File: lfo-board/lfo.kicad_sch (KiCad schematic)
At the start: 21 parts

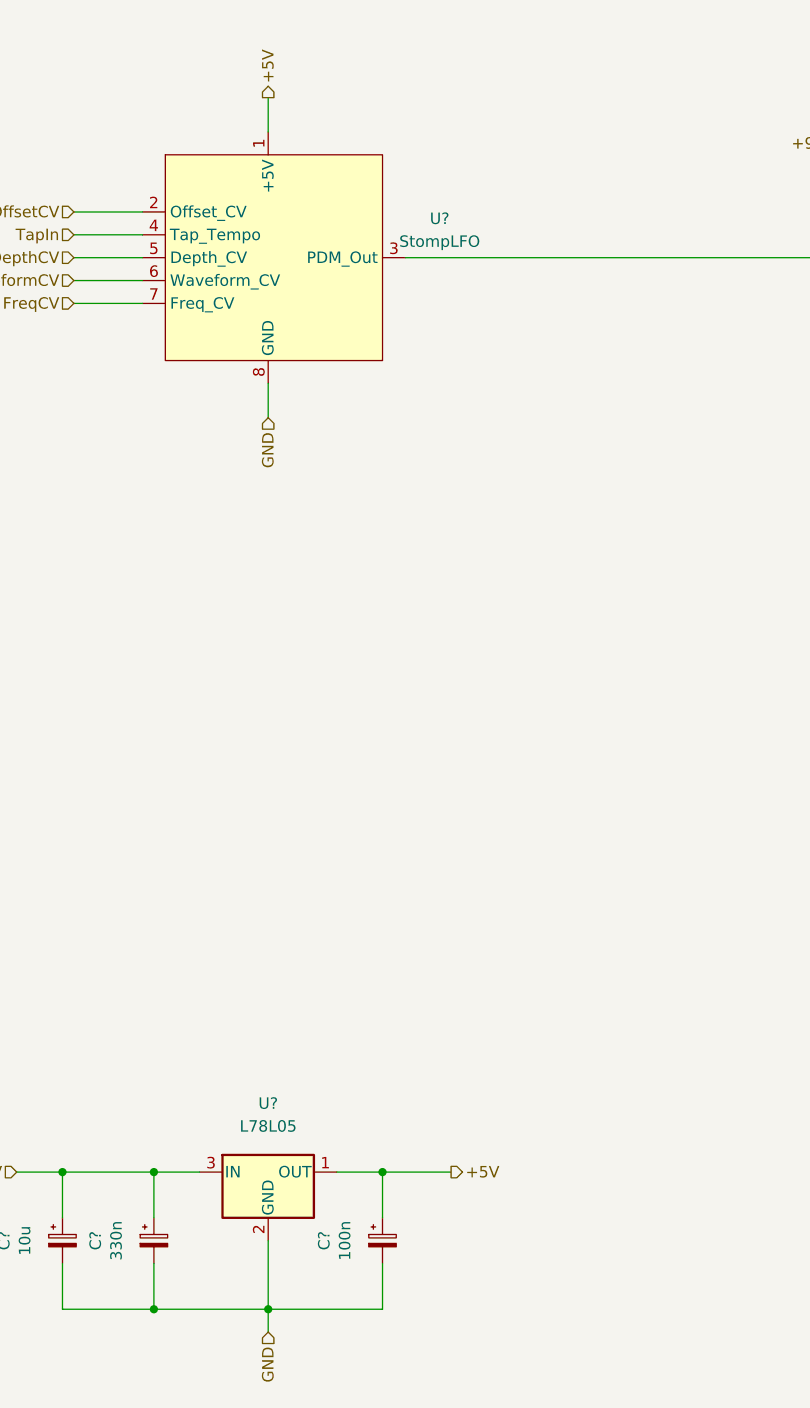
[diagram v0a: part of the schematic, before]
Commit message: IO Board wip
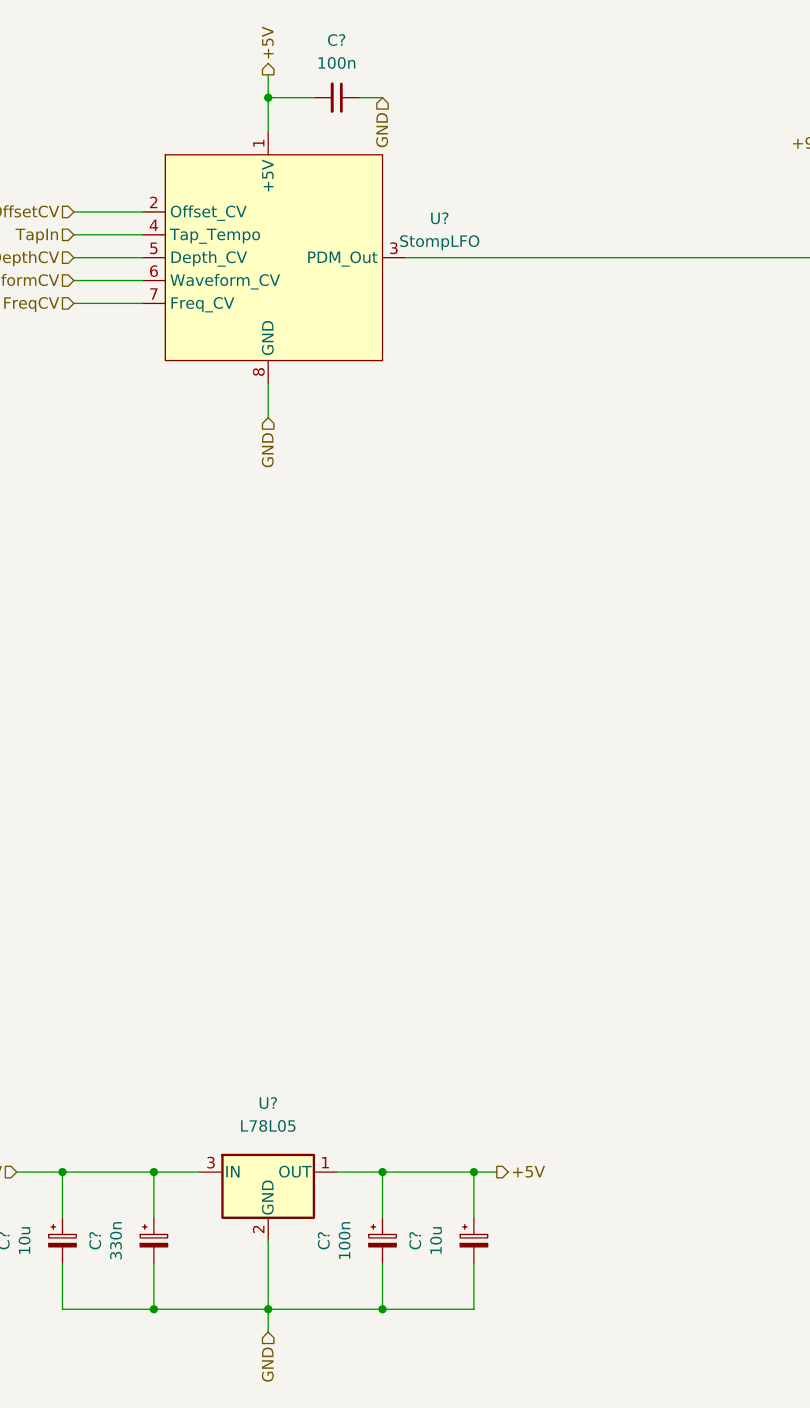
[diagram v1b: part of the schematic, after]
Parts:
- added C?: 10u, Capacitor_Tantalum_SMD:CP_EIA-3216-10_Kemet-I_Pad1.58x1.35mm_HandSolder, symbol Device:C_Polarized_Small
- added C?: 100n, symbol Device:C_Small
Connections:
- net +5V: now also C?.1, C?.2
- net GND: now also C?.1, C?.2
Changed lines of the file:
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@@
   (junction (at 66.04 152.4) (diameter 0) (color 0 0 0 0)
   )
+  (junction (at 91.44 167.64) (diameter 0) (color 0 0 0 0)
+  )
+  (junction (at 78.74 33.02) (diameter 0) (color 0 0 0 0)
+  )
   (junction (at 170.18 50.8) (diameter 0) (color 0 0 0 0)
   )
@@
   (junction (at 203.2 53.34) (diameter 0) (color 0 0 0 0)
   )
+  (junction (at 101.6 152.4) (diameter 0) (color 0 0 0 0)
+  )
   (junction (at 193.04 66.04) (diameter 0) (color 0 0 0 0)
   )
@@
     (stroke (width 0) (type default) (color 0 0 0 0))
   )
+  (wire (pts (xy 101.6 152.4) (xy 101.6 157.48))
+    (stroke (width 0) (type default) (color 0 0 0 0))
+  )
   (wire (pts (xy 154.94 50.8) (xy 160.02 50.8))
     (stroke (width 0) (type default) (color 0 0 0 0))
@@
     (stroke (width 0) (type default) (color 0 0 0 0))
   )
-  (wire (pts (xy 91.44 152.4) (xy 99.06 152.4))
+  (wire (pts (xy 91.44 152.4) (xy 101.6 152.4))
     (stroke (width 0) (type default) (color 0 0 0 0))
   )
@@
     (stroke (width 0) (type default) (color 0 0 0 0))
   )
+  (wire (pts (xy 101.6 167.64) (xy 91.44 167.64))
+    (stroke (width 0) (type default) (color 0 0 0 0))
+  )
   (wire (pts (xy 182.88 109.22) (xy 177.8 109.22))
     (stroke (width 0) (type default) (color 0 0 0 0))
   )
+  (wire (pts (xy 78.74 33.02) (xy 83.82 33.02))
+    (stroke (width 0) (type default) (color 0 0 0 0))
+  )
   (wire (pts (xy 187.96 109.22) (xy 193.04 109.22))
     (stroke (width 0) (type default) (color 0 0 0 0))
   )
+  (wire (pts (xy 101.6 162.56) (xy 101.6 167.64))
+    (stroke (width 0) (type default) (color 0 0 0 0))
+  )
+  (wire (pts (xy 88.9 33.02) (xy 91.44 33.02))
+    (stroke (width 0) (type default) (color 0 0 0 0))
+  )
+  (wire (pts (xy 78.74 30.48) (xy 78.74 33.02))
+    (stroke (width 0) (type default) (color 0 0 0 0))
+  )
+  (wire (pts (xy 170.18 50.8) (xy 177.8 50.8))
+    (stroke (width 0) (type default) (color 0 0 0 0))
+  )
+  (wire (pts (xy 187.96 99.06) (xy 193.04 99.06))
+    (stroke (width 0) (type default) (color 0 0 0 0))
+  )
+  (wire (pts (xy 193.04 99.06) (xy 193.04 109.22))
+    (stroke (width 0) (type default) (color 0 0 0 0))
+  )
+  (wire (pts (xy 256.54 60.96) (xy 266.7 60.96))
+    (stroke (width 0) (type default) (color 0 0 0 0))
+  )
+  (wire (pts (xy 193.04 66.04) (xy 193.04 63.5))
+    (stroke (width 0) (type default) (color 0 0 0 0))
+  )
+  (wire (pts (xy 172.72 124.46) (xy 177.8 124.46))
+    (stroke (width 0) (type default) (color 0 0 0 0))
+  )
+  (wire (pts (xy 203.2 63.5) (xy 210.82 63.5))
+    (stroke (width 0) (type default) (color 0 0 0 0))
+  )
   (wire (pts (xy 78.74 33.02) (xy 78.74 36.83))
     (stroke (width 0) (type default) (color 0 0 0 0))
   )
-  (wire (pts (xy 170.18 50.8) (xy 177.8 50.8))
-    (stroke (width 0) (type default) (color 0 0 0 0))
-  )
-  (wire (pts (xy 187.96 99.06) (xy 193.04 99.06))
-    (stroke (width 0) (type default) (color 0 0 0 0))
-  )
-  (wire (pts (xy 193.04 99.06) (xy 193.04 109.22))
-    (stroke (width 0) (type default) (color 0 0 0 0))
-  )
-  (wire (pts (xy 256.54 60.96) (xy 266.7 60.96))
-    (stroke (width 0) (type default) (color 0 0 0 0))
-  )
-  (wire (pts (xy 193.04 66.04) (xy 193.04 63.5))
-    (stroke (width 0) (type default) (color 0 0 0 0))
-  )
-  (wire (pts (xy 172.72 124.46) (xy 177.8 124.46))
-    (stroke (width 0) (type default) (color 0 0 0 0))
-  )
-  (wire (pts (xy 203.2 63.5) (xy 210.82 63.5))
-    (stroke (width 0) (type default) (color 0 0 0 0))
-  )
   (wire (pts (xy 55.88 167.64) (xy 66.04 167.64))
+    (stroke (width 0) (type default) (color 0 0 0 0))
+  )
+  (wire (pts (xy 101.6 152.4) (xy 104.14 152.4))
     (stroke (width 0) (type default) (color 0 0 0 0))
   )
@@
     (effects (font (size 1.27 1.27)) (justify right))
   )
+  (hierarchical_label "GND" (shape input) (at 91.44 33.02 270)
+    (effects (font (size 1.27 1.27)) (justify right))
+  )
   (hierarchical_label "Out" (shape input) (at 220.98 53.34 0)
     (effects (font (size 1.27 1.27)) (justify left))
@@
     (effects (font (size 1.27 1.27)) (justify left))
   )
-  (hierarchical_label "+5V" (shape output) (at 78.74 33.02 90)
+  (hierarchical_label "+5V" (shape output) (at 78.74 30.48 90)
     (effects (font (size 1.27 1.27)) (justify left))
   )
@@
     (effects (font (size 1.27 1.27)) (justify right))
   )
-  (hierarchical_label "+5V" (shape output) (at 99.06 152.4 0)
+  (hierarchical_label "+5V" (shape output) (at 104.14 152.4 0)
     (effects (font (size 1.27 1.27)) (justify left))
   )
@@
     )
     (property "Datasheet" "~" (id 3) (at 193.04 71.12 0)
+      (effects (font (size 1.27 1.27)) hide)
+    )
+    (pin "1")
+    (pin "2")
+  )
+  (symbol (lib_id "Device:C_Polarized_Small") (at 101.6 160.02 0) (unit 1)
+    (in_bom yes) (on_board yes)
+    (property "Reference" "C?" (id 0) (at 95.123 160.02 90))
+    (property "Value" "10u" (id 1) (at 97.4344 160.02 90))
+    (property "Footprint" "Capacitor_Tantalum_SMD:CP_EIA-3216-10_Kemet-I_Pad1.58x1.35mm_HandSolder" (id 2) (at 101.6 160.02 0)
+      (effects (font (size 1.27 1.27)) hide)
+    )
+    (property "Datasheet" "~" (id 3) (at 101.6 160.02 0)
+      (effects (font (size 1.27 1.27)) hide)
+    )
+    (property "LCSC" "C128254" (id 4) (at 101.6 160.02 0)
+      (effects (font (size 1.27 1.27)) hide)
+    )
+    (property "Role" "" (id 5) (at 101.6 160.02 0)
+      (effects (font (size 1.27 1.27)) hide)
+    )
+    (property "Mouser" "" (id 6) (at 101.6 160.02 0)
       (effects (font (size 1.27 1.27)) hide)
     )
@@
       (effects (font (size 1.27 1.27)) hide)
     )
+    (pin "1")
+    (pin "2")
+  )
+  (symbol (lib_id "Device:C_Small") (at 86.36 33.02 270) (unit 1)
+    (in_bom yes) (on_board yes) (fields_autoplaced)
+    (property "Reference" "C?" (id 0) (at 86.3536 26.67 90))
+    (property "Value" "100n" (id 1) (at 86.3536 29.21 90))
+    (property "Footprint" "" (id 2) (at 86.36 33.02 0)
+      (effects (font (size 1.27 1.27)) hide)
+    )
+    (property "Datasheet" "~" (id 3) (at 86.36 33.02 0)
+      (effects (font (size 1.27 1.27)) hide)
+    )

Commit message: wip
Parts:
- removed C?: 47n, symbol Device:C_Small
- removed R?: 1K, symbol Device:R_Small
- removed R?: 100K, symbol Device:R_Small
- added D2: LED_Dual_Bidirectional, LED_SMD:LED_0603_1608Metric_Pad1.05x0.95mm_HandSolder, symbol Device:LED_Dual_Bidirectional
- added R34: 470, Resistor_SMD:R_0603_1608Metric_Pad0.98x0.95mm_HandSolder, symbol Device:R_Small
- added R35: 20K, Resistor_SMD:R_0603_1608Metric_Pad0.98x0.95mm_HandSolder, symbol Device:R_Small
- C14, C17, C18, C19: renamed from C?; footprint (none) -> Capacitor_SMD:C_0603_1608Metric_Pad1.08x0.95mm_HandSolder
- R30, R31, R32, R33, R36, R37, R38: renamed from R?; footprint (none) -> Resistor_SMD:R_0603_1608Metric_Pad0.98x0.95mm_HandSolder
- U4, U6: renamed from U?; footprint (none) -> Package_SO:SOIC-8_3.9x4.9mm_P1.27mm
- gave numbers to parts that had none: 5
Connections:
- net +4.5V: now also R34.2, R35.1; no longer U6.5 (+)
- net at U6.6 (-): now also D2.2 (AK), R34.1; no longer R33.2
- net at U6.7: now also D2.1 (KA)
- new net: R33.2, R35.2, U6.5 (+)
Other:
- moved on the sheet: R33

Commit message: LFO graphics
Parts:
- C17: value 10n -> 6.8n
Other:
- note added: "C17 is 10n in the doc, switched due to tests w/ Konstrukt"
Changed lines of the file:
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@@
     (stroke (width 0) (type default) (color 0 0 0 0))
+  )
+  (text "C17 is 10n in the doc,\nswitched due to tests w/ Konstrukt"
+    (at 161.29 29.21 0)
+    (effects (font (size 1.27 1.27)) (justify left bottom))
   )
   (label "LFOFiltered" (at 162.56 124.46 180)
@@
     (in_bom yes) (on_board yes) (fields_autoplaced)
     (property "Reference" "C17" (id 0) (at 162.5663 31.75 90))
-    (property "Value" "10n" (id 1) (at 162.5663 34.29 90))
+    (property "Value" "6.8n" (id 1) (at 162.5663 34.29 90))
     (property "Footprint" "Capacitor_SMD:C_0603_1608Metric_Pad1.08x0.95mm_HandSolder" (id 2) (at 162.56 38.1 0)
       (effects (font (size 1.27 1.27)) hide)

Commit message: wip attenuverters
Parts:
- D2: footprint LED_SMD:LED_0603_1608Metric_Pad1.05x0.95mm_HandSolder -> LED_THT:LED_D3.0mm
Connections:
- net at R34.1, U6.6 (-): now also D2.1 (KA); no longer D2.2 (AK)
- net at U6.7: now also D2.2 (AK); no longer D2.1 (KA)
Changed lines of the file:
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@@
     (pin "2")
   )
-  (symbol (lib_id "Device:LED_Dual_Bidirectional") (at 185.42 99.06 0) (unit 1)
+  (symbol (lib_id "Device:LED_Dual_Bidirectional") (at 185.42 99.06 0) (mirror y) (unit 1)
     (in_bom yes) (on_board yes) (fields_autoplaced)
-    (property "Reference" "D2" (id 0) (at 185.9153 87.63 0))
-    (property "Value" "LED_Dual_Bidirectional" (id 1) (at 185.9153 90.17 0))
-    (property "Footprint" "LED_SMD:LED_0603_1608Metric_Pad1.05x0.95mm_HandSolder" (id 2) (at 185.42 99.06 0)
+    (property "Reference" "D2" (id 0) (at 184.9247 87.63 0))
+    (property "Value" "LED_Dual_Bidirectional" (id 1) (at 184.9247 90.17 0))
+    (property "Footprint" "LED_THT:LED_D3.0mm" (id 2) (at 185.42 99.06 0)
       (effects (font (size 1.27 1.27)) hide)
     )

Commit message: LFO board jlc
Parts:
- C14, C19: LCSC (none) -> C497032
- C17: value 6.8n -> 10n; LCSC (none) -> C57112
- C18: LCSC (none) -> C85980
- R30: LCSC (none) -> C23137
- R31: LCSC (none) -> C23242
- R32, R35: LCSC (none) -> C4184
- R33, R37: LCSC (none) -> C25803
- R34: value 470 -> 1k; LCSC (none) -> C21190
- R36: LCSC (none) -> C23352
- R38: LCSC (none) -> C21190
- U6: LCSC (none) -> C46127
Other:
- note removed: "C17 is 10n in the doc, switched due to tests w/ Konstrukt"
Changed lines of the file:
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@@
     (stroke (width 0) (type default) (color 0 0 0 0))
-  )
-  (text "C17 is 10n in the doc,\nswitched due to tests w/ Konstrukt"
-    (at 161.29 29.21 0)
-    (effects (font (size 1.27 1.27)) (justify left bottom))
   )
   (label "LFOFiltered" (at 162.56 124.46 180)
@@
     )
     (property "Datasheet" "~" (id 3) (at 193.04 71.12 0)
+      (effects (font (size 1.27 1.27)) hide)
+    )
+    (property "LCSC" "C25803" (id 4) (at 193.04 71.12 0)
       (effects (font (size 1.27 1.27)) hide)
     )
@@
       (effects (font (size 1.27 1.27)) hide)
     )
+    (property "LCSC" "C23137" (id 4) (at 149.86 38.1 0)
+      (effects (font (size 1.27 1.27)) hide)
+    )
     (pin "1")
     (pin "2")
@@
     )
     (property "Datasheet" "~" (id 3) (at 193.04 60.96 0)
+      (effects (font (size 1.27 1.27)) hide)
+    )
+    (property "LCSC" "C23352" (id 4) (at 193.04 60.96 0)
       (effects (font (size 1.27 1.27)) hide)
     )
@@
     (in_bom yes) (on_board yes) (fields_autoplaced)
     (property "Reference" "R34" (id 0) (at 171.45 92.71 90))
-    (property "Value" "470" (id 1) (at 171.45 95.25 90))
+    (property "Value" "1k" (id 1) (at 171.45 95.25 90))
     (property "Footprint" "Resistor_SMD:R_0603_1608Metric_Pad0.98x0.95mm_HandSolder" (id 2) (at 171.45 99.06 0)
       (effects (font (size 1.27 1.27)) hide)
     )
     (property "Datasheet" "~" (id 3) (at 171.45 99.06 0)
+      (effects (font (size 1.27 1.27)) hide)
+    )
+    (property "LCSC" "C21190" (id 4) (at 171.45 99.06 0)
       (effects (font (size 1.27 1.27)) hide)
     )
@@
     )
     (property "Datasheet" "~" (id 3) (at 269.24 53.34 0)
+      (effects (font (size 1.27 1.27)) hide)
+    )
+    (property "LCSC" "C46127" (id 4) (at 269.24 53.34 0)
       (effects (font (size 1.27 1.27)) hide)
     )
@@
       (effects (font (size 1.27 1.27)) hide)
     )
+    (property "LCSC" "C4184" (id 4) (at 162.56 50.8 0)
+      (effects (font (size 1.27 1.27)) hide)
+    )
     (pin "1")
     (pin "2")
@@
     )
     (property "Datasheet" "~" (id 3) (at 185.42 53.34 0)
+      (effects (font (size 1.27 1.27)) hide)
+    )
+    (property "LCSC" "C46127" (id 4) (at 185.42 53.34 0)
       (effects (font (size 1.27 1.27)) hide)
     )
@@
     (in_bom yes) (on_board yes) (fields_autoplaced)
     (property "Reference" "C17" (id 0) (at 162.5663 31.75 90))
-    (property "Value" "6.8n" (id 1) (at 162.5663 34.29 90))
+    (property "Value" "10n" (id 1) (at 162.5663 34.29 90))
     (property "Footprint" "Capacitor_SMD:C_0603_1608Metric_Pad1.08x0.95mm_HandSolder" (id 2) (at 162.56 38.1 0)
       (effects (font (size 1.27 1.27)) hide)
@@
       (effects (font (size 1.27 1.27)) hide)
     )
+    (property "LCSC" "C57112" (id 4) (at 162.56 38.1 0)
+      (effects (font (size 1.27 1.27)) hide)
+    )
     (pin "1")
     (pin "2")
@@
     )
     (property "Datasheet" "~" (id 3) (at 175.26 129.54 0)
+      (effects (font (size 1.27 1.27)) hide)
+    )
+    (property "LCSC" "C4184" (id 4) (at 175.26 129.54 0)
       (effects (font (size 1.27 1.27)) hide)
     )
@@
     )
     (property "Datasheet" "~" (id 3) (at 170.18 58.42 0)
+      (effects (font (size 1.27 1.27)) hide)
+    )
+    (property "LCSC" "C85980" (id 4) (at 170.18 58.42 0)
       (effects (font (size 1.27 1.27)) hide)
     )
@@
       (effects (font (size 1.27 1.27)) hide)
     )
+    (property "LCSC" "C23242" (id 4) (at 149.86 50.8 0)
+      (effects (font (size 1.27 1.27)) hide)
+    )
     (pin "1")
     (pin "2")
@@
     )
     (property "Datasheet" "~" (id 3) (at 86.36 33.02 0)
+      (effects (font (size 1.27 1.27)) hide)
+    )
+    (property "LCSC" "C497032" (id 4) (at 86.36 33.02 0)
       (effects (font (size 1.27 1.27)) hide)
     )
@@
       (effects (font (size 1.27 1.27)) hide)
     )
+    (property "LCSC" "C25803" (id 4) (at 170.18 124.46 0)
+      (effects (font (size 1.27 1.27)) hide)
+    )
     (pin "1")
     (pin "2")
@@
     )
     (property "Datasheet" "~" (id 3) (at 256.54 53.34 0)
+      (effects (font (size 1.27 1.27)) hide)
+    )
+    (property "LCSC" "C497032" (id 4) (at 256.54 53.34 0)
       (effects (font (size 1.27 1.27)) hide)
     )
@@
     )
     (property "Datasheet" "~" (id 3) (at 185.42 121.92 0)
+      (effects (font (size 1.27 1.27)) hide)
+    )
+    (property "LCSC" "C46127" (id 4) (at 185.42 121.92 0)
       (effects (font (size 1.27 1.27)) hide)
     )
@@
       (effects (font (size 1.27 1.27)) hide)
     )
+    (property "LCSC" "C21190" (id 4) (at 213.36 53.34 0)
+      (effects (font (size 1.27 1.27)) hide)
+    )

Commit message: wip
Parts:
- C15: LCSC C1952859 -> C7173
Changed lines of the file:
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@@
       (effects (font (size 1.27 1.27)) hide)
     )
-    (property "LCSC" "C1952859" (id 4) (at 91.44 160.02 0)
+    (property "LCSC" "C7173" (id 4) (at 91.44 160.02 0)
       (effects (font (size 1.27 1.27)) hide)
     )

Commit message: wip pre-redo orientation
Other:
- company: (none) -> Andrey Salomatin / Pedal Markt
- title: (none) -> Longwave
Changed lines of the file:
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@@
 (kicad_sch (version 20211123) (generator eeschema)
   (paper "A4")
+  (title_block
+    (title "Longwave")
+    (date "2024-12-18")
+    (rev "v1rev2")
+    (company "Andrey Salomatin / Pedal Markt")
+  )
   (junction (at 66.04 167.64) (diameter 0) (color 0 0 0 0)
   )
